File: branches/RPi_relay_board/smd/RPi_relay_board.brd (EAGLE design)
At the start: 81 x 88.3 mm, 48 parts, among them IC1 LM340S-05, K1 351, K2 351, T1 ZXTN2020F, T2 ZXTN2020F, T3 ZXTN2020F, U1 MAX232SOIC16

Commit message: Version 2.0-series of pcb
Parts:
- removed C10: 100nF, rcl:C2012
- removed C11: 10uF, rcl:C3216
- removed C12: 330nF, SparkFun:EIA7343
- removed IC1: LM340S-05, LM1084IS:TO263-3
- C4: value 330nF -> 100nF; device rcl:C3216 -> rcl:C2012
- C5: device rcl:C3216 -> rcl:C2012
- C9: value 100nF -> 330nF; device rcl:C2012 -> SparkFun:EIA7343
- moved C1 60.8 mm to (39.4, 0.00), turned to 180 degrees
- moved R1 55.4 mm to (35.6, 15.9), flipped to the top, turned to 270 degrees
- moved T3 52.9 mm to (31.1, 15.9), flipped to the top, turned to 90 degrees
- moved R2 48.5 mm to (69.7, 21.6), flipped to the top, turned to 0 degrees
- moved R3 40.5 mm to (69.7, 39.4), flipped to the top, turned to 0 degrees
- moved SJ1_GND 38.5 mm to (65.8, 23.8), turned to 90 degrees
- moved C4 35.6 mm to (66.1, 12.7), flipped to the top, turned to 90 degrees
- moved OK2 35.5 mm to (64.7, 44.2), flipped to the top, turned to 180 degrees
- moved C9 34.7 mm to (39.4, 6.35), flipped to the top, turned to 180 degrees
- moved OK1 34.3 mm to (64.7, 26.4), flipped to the top, turned to 180 degrees
- moved R5 32.9 mm to (69.5, 44.8), flipped to the top, turned to 90 degrees
- moved R4 31.4 mm to (69.5, 27.0), flipped to the top, turned to 90 degrees
- moved SJ1_12V 31.4 mm to (62.0, 23.8), turned to 90 degrees
- moved OK3 30.8 mm to (28.9, 26.6), turned to 180 degrees
- moved T2 29.6 mm to (33.9, 40.6)
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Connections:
- net +12V: no longer C4.1, IC1.3
- net +5V: no longer C3.1, IC1.2, IC1.TAB
- net 3.3V: now also C3.1, C4.2, C6.1; no longer C5.1, C6.2, C8.1
- net GND: now also C6.2, C9.C; no longer C11.2, C12.C, C4.2, C7.2, C8.2, IC1.1
- net N$10: now also C9.A; no longer C11.1, C12.A
- net N$13: now also C7.2; no longer C9.2
- net N$31: now also C8.2; no longer C10.2
- net N$32: now also C7.1; no longer C9.1
- net N$35: now also C8.1; no longer C10.1
- net N$36: now also C4.1; no longer C6.1
- net N$37: now also C5.1; no longer C7.1
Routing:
- net +12V: track 225.0 -> 118.3 mm
- net N$3: track 103.1 -> 20.3 mm
- net N$5: track 99.8 -> 29.8 mm
- net N$15: track 127.5 -> 63.3 mm
- net N$20: track 57.1 -> 11.0 mm
- net GND: track 39.2 -> 83.6 mm
- net N$51: track 47.3 -> 3.35 mm
- net N$18: track 51.8 -> 11.0 mm
- net N$4: track 26.9 -> 64.8 mm, vias 1 -> 3
- net 3.3V: track 171.1 -> 138.6 mm, vias 0 -> 1
- net N$1: track 35.3 -> 61.3 mm
- net N$19: track 21.9 -> 3.35 mm
- net N$12: track 26.1 -> 8.18 mm
- net N$16: track 35.1 -> 21.1 mm, vias 0 -> 1
- net N$44: track 22.1 -> 8.39 mm
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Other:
- board size 81 x 88.3 mm -> 75.9 x 61.6 mm
- board text added: "(c) Kristoffer Ek stoffer@skulp.net"
- board text added: "12V"
- board text added: "5V"
- board text added: "GND"
- board text added: "INPUT 1"
- board text added: "INPUT 2"
- board text added: "OpenLock RPi RFID lock interface v.2.1 2013"
- board text added: "RELAY 1"
- board text added: "RELAY 2"
- board text added: "RFID"
- board text removed: "OUTPUT 1"
- board text removed: "OUTPUT 2"
- board text removed: "OpenLock RPi RFID lock interface v.1.9.1 2013"

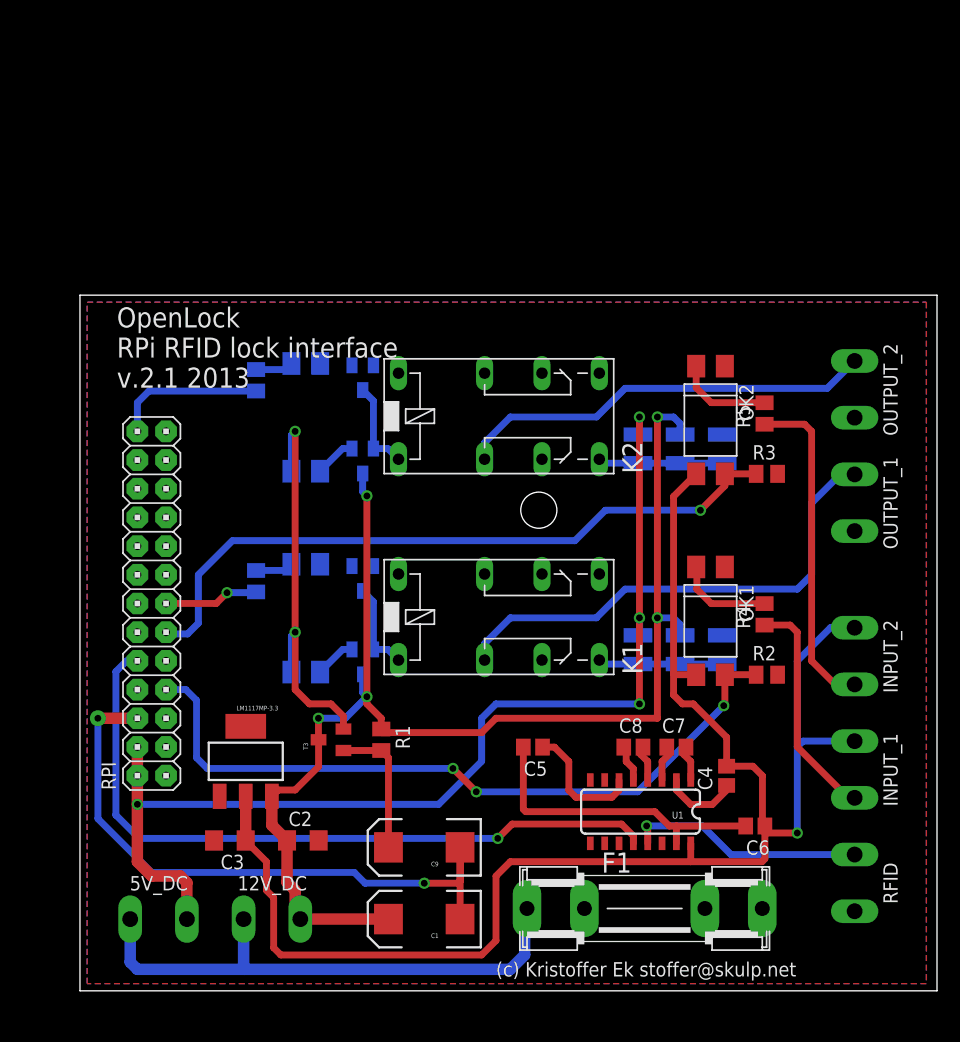
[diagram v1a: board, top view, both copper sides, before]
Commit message: input opto's was wrong polarity on output
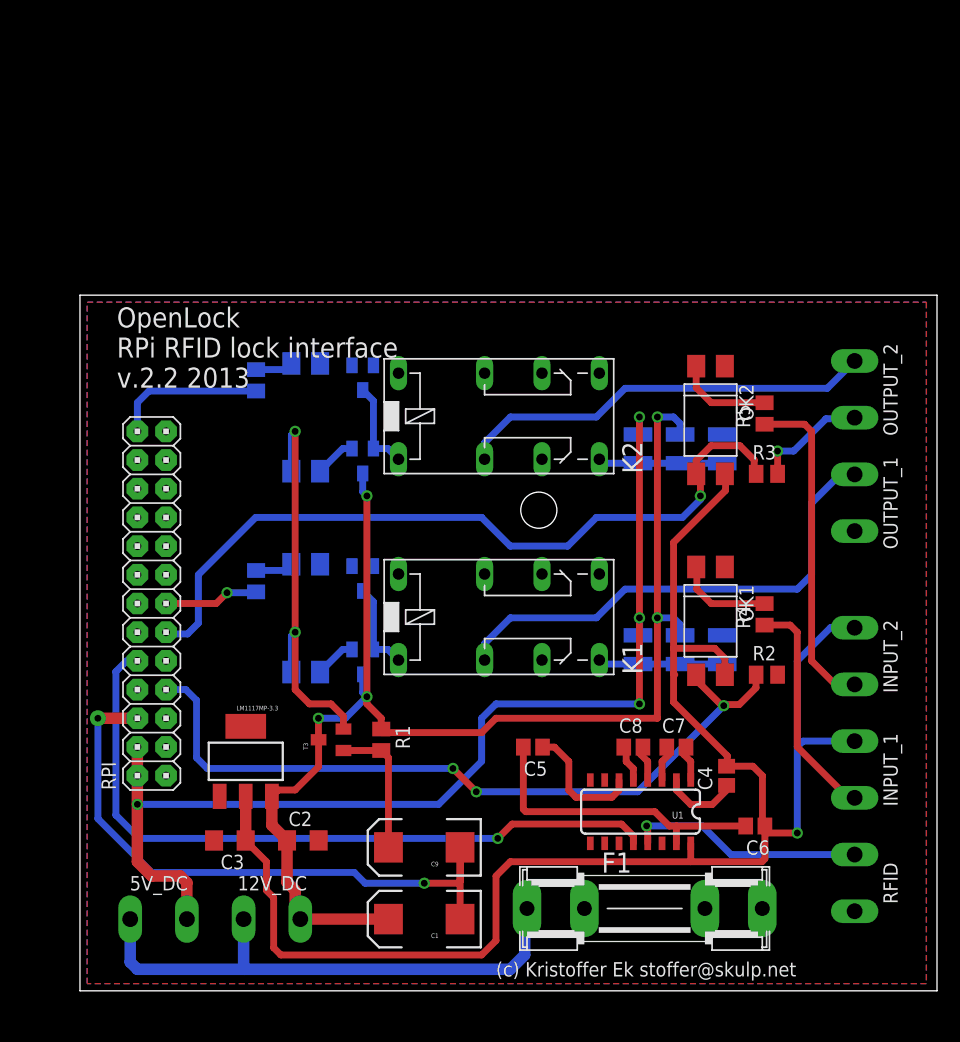
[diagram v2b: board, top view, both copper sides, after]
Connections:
- net 3.3V: now also OK1.4, OK2.4; no longer OK1.3, OK2.3
- net N$1: now also OK2.3; no longer OK2.4
- net N$4: now also OK1.3; no longer OK1.4
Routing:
- net GND: track 83.6 -> 93.6 mm, vias 2 -> 3
- net N$1: track 61.3 -> 68.0 mm
- net 3.3V: track 138.6 -> 143.7 mm
- net N$4: track 64.8 -> 68.1 mm
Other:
- board text added: "OpenLock RPi RFID lock interface v.2.2 2013"
- board text removed: "OpenLock RPi RFID lock interface v.2.1 2013"
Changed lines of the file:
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@@
 <setting verticaltext="up"/>
 </settings>
-<grid distance="0.05" unitdist="inch" unit="inch" style="dots" multiple="1" display="no" altdistance="0.025" altunitdist="inch" altunit="inch"/>
+<grid distance="0.00625" unitdist="inch" unit="inch" style="dots" multiple="1" display="no" altdistance="0.0125" altunitdist="inch" altunit="inch"/>
 <layers>
 <layer number="1" name="Top" color="4" fill="1" visible="yes" active="yes"/>
@@
 <text x="12.15279375" y="47.04260625" size="1.778" layer="25">OpenLock
 RPi RFID lock interface
-v.2.1 2013</text>
+v.2.2 2013</text>
 <hole x="49.51" y="36.2" drill="3.2"/>
 <text x="13.335" y="-5.08" size="1.27" layer="26" rot="MR0" align="bottom-center">GND</text>
@@
 <wire x1="15.24" y1="4.1275" x2="10.4775" y2="8.89" width="0.6096" layer="16"/>
 <wire x1="10.4775" y1="8.89" x2="10.4775" y2="17.78" width="0.6096" layer="16"/>
+<wire x1="70.649321875" y1="39.415365625" x2="70.649321875" y2="41.428178125" width="0.6096" layer="1"/>
+<wire x1="70.649321875" y1="41.428178125" x2="70.64375" y2="41.43375" width="0.6096" layer="1"/>
+<via x="70.64375" y="41.43375" extent="1-16" drill="0.6"/>
+<wire x1="70.64375" y1="41.43375" x2="72.0725" y2="41.43375" width="0.6096" layer="16"/>
+<wire x1="72.0725" y1="41.43375" x2="74.93" y2="44.29125" width="0.6096" layer="16"/>
+<wire x1="74.93" y1="44.29125" x2="77.37125" y2="44.29125" width="0.6096" layer="16"/>
+<wire x1="77.37125" y1="44.29125" x2="77.47" y2="44.39" width="0.6096" layer="16"/>
 </signal>
 <signal name="N$51">
@@
 </signal>
 <signal name="N$1">
-<contactref element="R3" pad="1"/>
 <contactref element="RPI" pad="11"/>
-<contactref element="OK2" pad="4"/>
-<wire x1="65.98115625" y1="39.415365625" x2="68.749321875" y2="39.415365625" width="0.6096" layer="1"/>
-<wire x1="65.98115625" y1="39.415365625" x2="65.98115625" y2="38.35865625" width="0.6096" layer="1"/>
-<wire x1="65.98115625" y1="38.35865625" x2="63.8175" y2="36.195" width="0.6096" layer="1"/>
-<via x="63.8175" y="36.195" extent="1-16" drill="0.6"/>
-<wire x1="63.8175" y1="36.195" x2="55.40375" y2="36.195" width="0.6096" layer="16"/>
-<wire x1="55.40375" y1="36.195" x2="52.705" y2="33.49625" width="0.6096" layer="16"/>
-<wire x1="52.705" y1="33.49625" x2="22.38375" y2="33.49625" width="0.6096" layer="16"/>
-<wire x1="22.38375" y1="33.49625" x2="19.3675" y2="30.48" width="0.6096" layer="16"/>
+<via x="63.8175" y="37.465" extent="1-16" drill="0.6"/>
+<wire x1="63.8175" y1="37.465" x2="63.8175" y2="37.1475" width="0.6096" layer="16"/>
+<wire x1="63.8175" y1="37.1475" x2="62.23" y2="35.56" width="0.6096" layer="16"/>
 <wire x1="19.3675" y1="30.48" x2="19.3675" y2="26.19375" width="0.6096" layer="16"/>
 <wire x1="19.3675" y1="26.19375" x2="18.415" y2="25.24125" width="0.6096" layer="16"/>
 <wire x1="18.415" y1="25.24125" x2="16.66875" y2="25.24125" width="0.6096" layer="16"/>
 <wire x1="16.66875" y1="25.24125" x2="16.51" y2="25.4" width="0.6096" layer="16"/>
+<contactref element="OK2" pad="3"/>
+<contactref element="R3" pad="1"/>
+<wire x1="63.44115625" y1="39.415365625" x2="63.44115625" y2="40.58115625" width="0.6096" layer="1"/>
+<wire x1="63.44115625" y1="40.58115625" x2="64.77" y2="41.91" width="0.6096" layer="1"/>
+<wire x1="64.77" y1="41.91" x2="67.31" y2="41.91" width="0.6096" layer="1"/>
+<wire x1="67.31" y1="41.91" x2="68.58" y2="40.64" width="0.6096" layer="1"/>
+<wire x1="68.58" y1="40.64" x2="68.58" y2="39.5846875" width="0.6096" layer="1"/>
+<wire x1="68.58" y1="39.5846875" x2="68.749321875" y2="39.415365625" width="0.6096" layer="1"/>
+<wire x1="54.61" y1="35.56" x2="62.23" y2="35.56" width="0.6096" layer="16"/>
+<wire x1="54.61" y1="35.56" x2="52.07" y2="33.02" width="0.6096" layer="16"/>
+<wire x1="52.07" y1="33.02" x2="46.99" y2="33.02" width="0.6096" layer="16"/>
+<wire x1="46.99" y1="33.02" x2="44.45" y2="35.56" width="0.6096" layer="16"/>
+<wire x1="44.45" y1="35.56" x2="24.4475" y2="35.56" width="0.6096" layer="16"/>
+<wire x1="24.4475" y1="35.56" x2="19.3675" y2="30.48" width="0.6096" layer="16"/>
+<wire x1="63.44115625" y1="39.415365625" x2="63.44115625" y2="39.27009375" width="0.6096" layer="1"/>
+<wire x1="63.44115625" y1="39.27009375" x2="63.8175" y2="38.89375" width="0.6096" layer="1"/>
+<wire x1="63.8175" y1="38.89375" x2="63.8175" y2="37.465" width="0.6096" layer="1"/>
 </signal>
 <signal name="N$4">
 <contactref element="R2" pad="1"/>
 <contactref element="RPI" pad="7"/>
-<contactref element="OK1" pad="4"/>
-<wire x1="68.749321875" y1="21.635365625" x2="65.98115625" y2="21.635365625" width="0.6096" layer="1"/>
-<wire x1="65.98115625" y1="21.635365625" x2="65.98115625" y2="18.99115625" width="0.6096" layer="1"/>
 <wire x1="65.98115625" y1="18.99115625" x2="65.88125" y2="18.89125" width="0.6096" layer="1"/>
 <via x="65.88125" y="18.89125" extent="1-16" drill="0.6"/>
@@
 <wire x1="19.20875" y1="19.3675" x2="18.25625" y2="20.32" width="0.6096" layer="16"/>
 <wire x1="18.25625" y1="20.32" x2="16.51" y2="20.32" width="0.6096" layer="16"/>
+<contactref element="OK1" pad="3"/>
+<wire x1="63.44115625" y1="21.635365625" x2="63.44115625" y2="21.33134375" width="0.6096" layer="1"/>
+<wire x1="65.98115625" y1="18.99115625" x2="67.25115625" y2="18.99115625" width="0.6096" layer="1"/>
+<wire x1="67.25115625" y1="18.99115625" x2="68.73875" y2="20.47875" width="0.6096" layer="1"/>
+<wire x1="68.73875" y1="20.47875" x2="68.73875" y2="21.62479375" width="0.6096" layer="1"/>
+<wire x1="68.73875" y1="21.62479375" x2="68.749321875" y2="21.635365625" width="0.6096" layer="1"/>
+<wire x1="65.88125" y1="18.89125" x2="65.7225" y2="18.89125" width="0.6096" layer="1"/>
+<wire x1="65.7225" y1="18.89125" x2="63.8175" y2="20.79625" width="0.6096" layer="1"/>
+<wire x1="63.8175" y1="20.79625" x2="63.8175" y2="21.259021875" width="0.6096" layer="1"/>
+<wire x1="63.8175" y1="21.259021875" x2="63.44115625" y2="21.635365625" width="0.6096" layer="1"/>
 </signal>
 <signal name="N$3">
@@
 <contactref element="C3" pad="1"/>
 <contactref element="U1" pad="16"/>
-<contactref element="OK1" pad="3"/>
-<contactref element="OK2" pad="3"/>
 <wire x1="66.134684375" y1="13.53455625" x2="68.459684375" y2="13.53455625" width="0.6096" layer="1"/>
 <wire x1="68.459684375" y1="13.53455625" x2="69.309684375" y2="12.68455625" width="0.6096" layer="1"/>
@@
 <wire x1="72.905" y1="15.755" x2="72.39" y2="15.24" width="0.6096" layer="16"/>
 <wire x1="72.39" y1="7.62" x2="69.524684375" y2="7.62" width="0.6096" layer="1"/>
-<wire x1="66.134684375" y1="13.53455625" x2="66.134684375" y2="16.097815625" width="0.6096" layer="1"/>
-<wire x1="66.134684375" y1="16.097815625" x2="63.1825" y2="19.05" width="0.6096" layer="1"/>
-<wire x1="63.1825" y1="19.05" x2="62.23" y2="19.05" width="0.6096" layer="1"/>
-<wire x1="62.23" y1="19.05" x2="61.43625" y2="19.84375" width="0.6096" layer="1"/>
-<wire x1="61.43625" y1="19.84375" x2="61.43625" y2="21.74875" width="0.6096" layer="1"/>
-<wire x1="61.43625" y1="21.74875" x2="61.43625" y2="37.410459375" width="0.6096" layer="1"/>
-<wire x1="61.43625" y1="37.410459375" x2="63.44115625" y2="39.415365625" width="0.6096" layer="1"/>
-<wire x1="63.44115625" y1="21.635365625" x2="61.549634375" y2="21.635365625" width="0.6096" layer="1"/>
+<wire x1="61.43625" y1="19.20875" x2="61.43625" y2="21.74875" width="0.6096" layer="1"/>
+<wire x1="61.43625" y1="21.74875" x2="61.43625" y2="23.97125" width="0.6096" layer="1"/>
+<wire x1="61.43625" y1="23.97125" x2="61.43625" y2="33.3375" width="0.6096" layer="1"/>
 <wire x1="61.549634375" y1="21.635365625" x2="61.43625" y2="21.74875" width="0.6096" layer="1"/>
+<contactref element="OK2" pad="4"/>
+<contactref element="OK1" pad="4"/>
+<wire x1="61.43625" y1="33.3375" x2="66.04" y2="37.94125" width="0.6096" layer="1"/>
+<wire x1="66.04" y1="37.94125" x2="66.04" y2="39.356521875" width="0.6096" layer="1"/>
+<wire x1="66.04" y1="39.356521875" x2="65.98115625" y2="39.415365625" width="0.6096" layer="1"/>
+<wire x1="65.98115625" y1="21.635365625" x2="65.98115625" y2="23.07759375" width="0.6096" layer="1"/>
+<wire x1="65.98115625" y1="23.07759375" x2="65.0875" y2="23.97125" width="0.6096" layer="1"/>
+<wire x1="65.0875" y1="23.97125" x2="61.43625" y2="23.97125" width="0.6096" layer="1"/>
+<wire x1="61.43625" y1="19.20875" x2="66.19875" y2="14.44625" width="0.6096" layer="1"/>
+<wire x1="66.19875" y1="14.44625" x2="66.19875" y2="13.598621875" width="0.6096" layer="1"/>
+<wire x1="66.19875" y1="13.598621875" x2="66.134684375" y2="13.53455625" width="0.6096" layer="1"/>
 </signal>
 <signal name="N$10">
@@
 </signal>
 </signals>
-<errors>
-</errors>
 </board>
 </drawing>

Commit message: small corrections
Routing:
- net +12V: track 118.3 -> 120.8 mm
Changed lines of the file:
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@@
 <wire x1="44.45" y1="16.51" x2="45.72" y2="17.78" width="0.6096" layer="1"/>
 <wire x1="45.72" y1="17.78" x2="60.0075" y2="17.78" width="0.6096" layer="1"/>
-<via x="60.0075" y="44.45" extent="1-16" drill="0.6"/>
+<via x="60.0075" y="45.4025" extent="1-16" drill="0.6"/>
 <wire x1="61.9125" y1="43.004671875" x2="62.01884375" y2="42.898328125" width="0.6096" layer="16"/>
-<wire x1="62.01884375" y1="42.898328125" x2="62.01884375" y2="43.86740625" width="0.6096" layer="16"/>
-<wire x1="62.01884375" y1="43.86740625" x2="61.43625" y2="44.45" width="0.6096" layer="16"/>
-<wire x1="61.43625" y1="44.45" x2="60.0075" y2="44.45" width="0.6096" layer="16"/>
-<wire x1="60.0075" y1="17.78" x2="60.0075" y2="26.67" width="0.6096" layer="1"/>
-<wire x1="60.0075" y1="26.67" x2="60.0075" y2="44.45" width="0.6096" layer="1"/>
-<wire x1="62.01884375" y1="25.118328125" x2="62.01884375" y2="26.08740625" width="0.6096" layer="16"/>
-<wire x1="62.01884375" y1="26.08740625" x2="61.43625" y2="26.67" width="0.6096" layer="16"/>
-<wire x1="61.43625" y1="26.67" x2="60.0075" y2="26.67" width="0.6096" layer="16"/>
-<via x="60.0075" y="26.67" extent="1-16" drill="0.6"/>
+<wire x1="62.01884375" y1="42.898328125" x2="62.01884375" y2="44.81990625" width="0.6096" layer="16"/>
+<wire x1="62.01884375" y1="44.81990625" x2="61.43625" y2="45.4025" width="0.6096" layer="16"/>
+<wire x1="61.43625" y1="45.4025" x2="60.0075" y2="45.4025" width="0.6096" layer="16"/>
+<wire x1="60.0075" y1="17.78" x2="60.0075" y2="27.46375" width="0.6096" layer="1"/>
+<wire x1="60.0075" y1="27.46375" x2="60.0075" y2="45.4025" width="0.6096" layer="1"/>
+<wire x1="62.01884375" y1="25.118328125" x2="62.01884375" y2="26.56365625" width="0.6096" layer="16"/>
+<wire x1="62.01884375" y1="26.56365625" x2="61.11875" y2="27.46375" width="0.6096" layer="16"/>
+<wire x1="61.11875" y1="27.46375" x2="60.0075" y2="27.46375" width="0.6096" layer="16"/>
+<via x="60.0075" y="27.46375" extent="1-16" drill="0.6"/>
 <wire x1="32.385" y1="17.78" x2="30.00375" y2="17.78" width="0.6096" layer="16"/>
 <via x="30.00375" y="17.78" extent="1-16" drill="0.6"/>
